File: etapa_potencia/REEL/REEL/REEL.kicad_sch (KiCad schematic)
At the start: 22 parts, among them SW1 SW_Push, SW2 SW_Reed, SW3 SW_Push, U2 ESP32-WROOM-32, U3 FT232

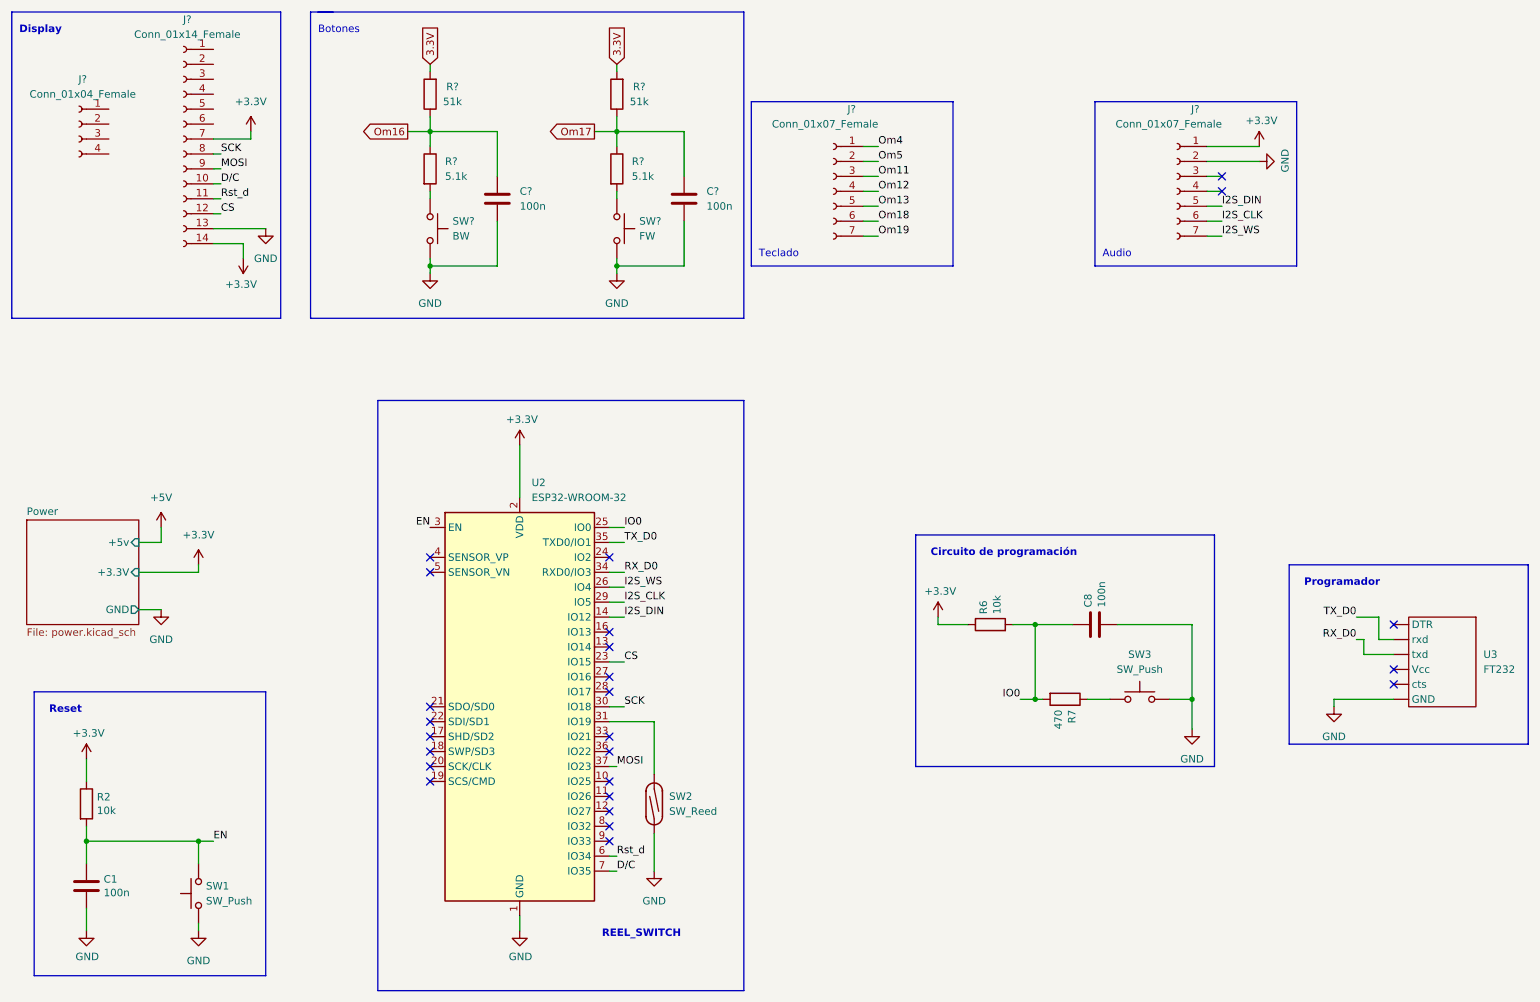
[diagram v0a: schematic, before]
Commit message: Edicion display y botones
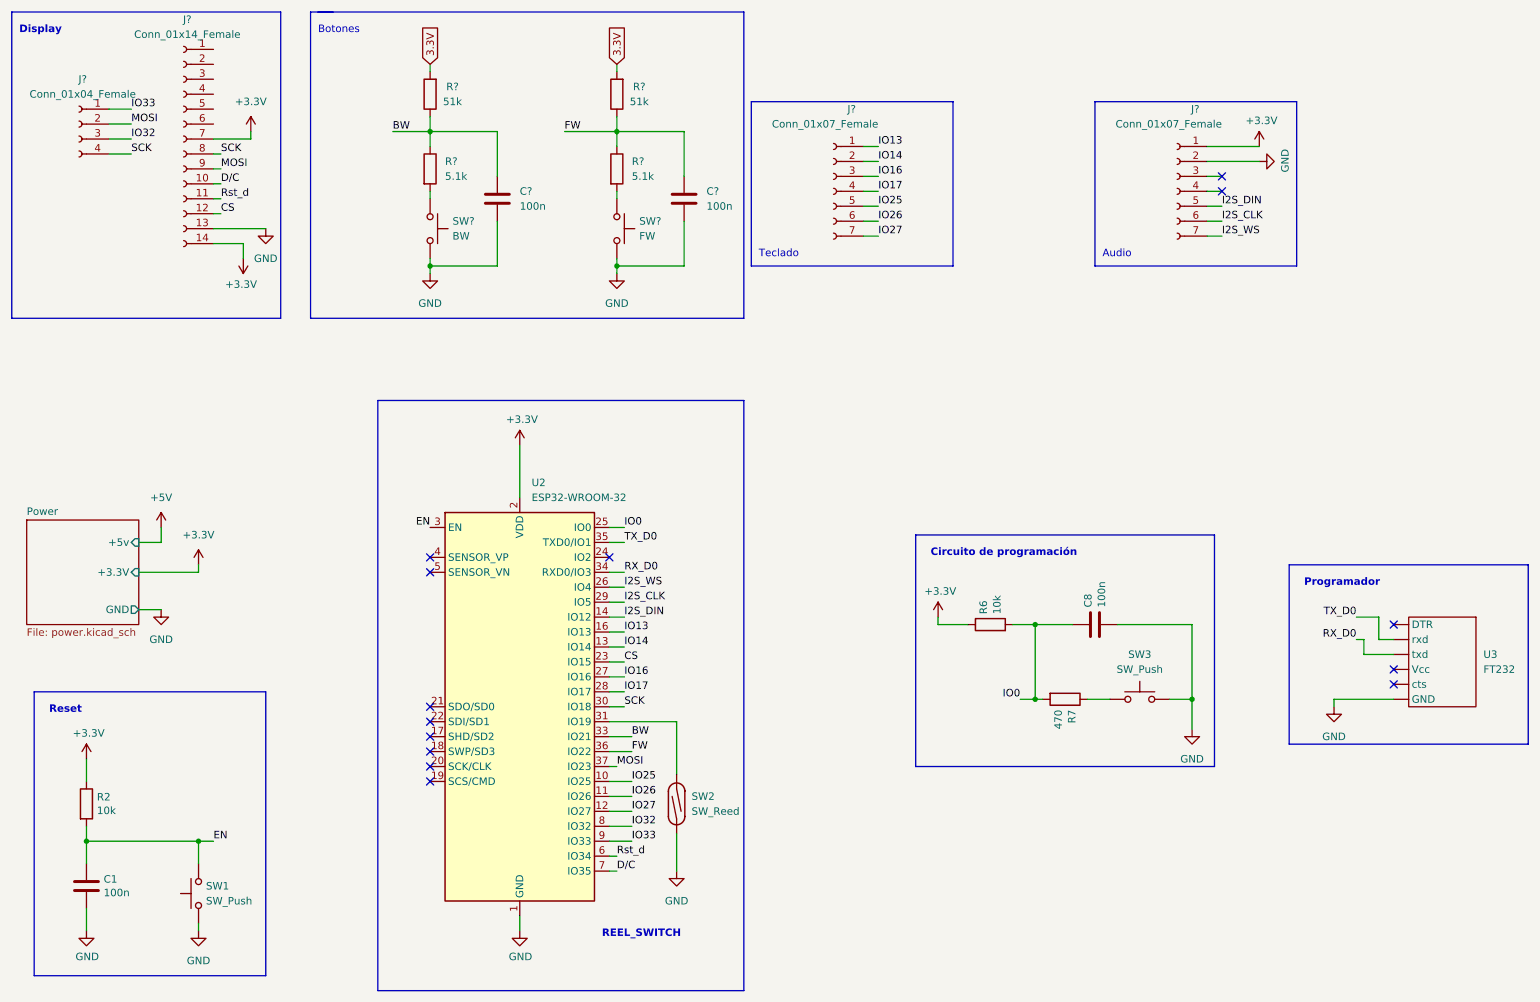
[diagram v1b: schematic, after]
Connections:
- net Om11 is gone; now on net IO16: J?.3 (Pin_3)
- net Om12 is gone; now on net IO17: J?.4 (Pin_4)
- net Om13 is gone; now on net IO25: J?.5 (Pin_5)
- net Om16 is gone; now on net BW: C?.2, R?.1, R?.1
- net Om17 is gone; now on net FW: C?.2, R?.1, R?.1
- net Om18 is gone; now on net IO26: J?.6 (Pin_6)
- net Om19 is gone; now on net IO27: J?.7 (Pin_7)
- net Om4 is gone; now on net IO13: J?.1 (Pin_1)
- net Om5 is gone; now on net IO14: J?.2 (Pin_2)
- net MOSI: now also J?.2 (Pin_2)
- net SCK: now also J?.4 (Pin_4)
- net IO25: now reaches U2.10 (IO25)
- net IO26: now reaches U2.11 (IO26)
- net IO27: now reaches U2.12 (IO27)
- net IO14: now reaches U2.13 (IO14)
- net IO13: now reaches U2.16 (IO13)
- net IO16: now reaches U2.27 (IO16)
- net IO17: now reaches U2.28 (IO17)
- net BW: now reaches U2.33 (IO21)
- net FW: now reaches U2.36 (IO22)
- net IO32: now reaches U2.8 (IO32)
- net IO32: now also J?.3 (Pin_3)
- net IO33: now reaches U2.9 (IO33)
- net IO33: now also J?.1 (Pin_1)
- no-connect marks 25 -> 14
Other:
- moved on the sheet: SW2

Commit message: Conexiones corregidas, PCB ordenada
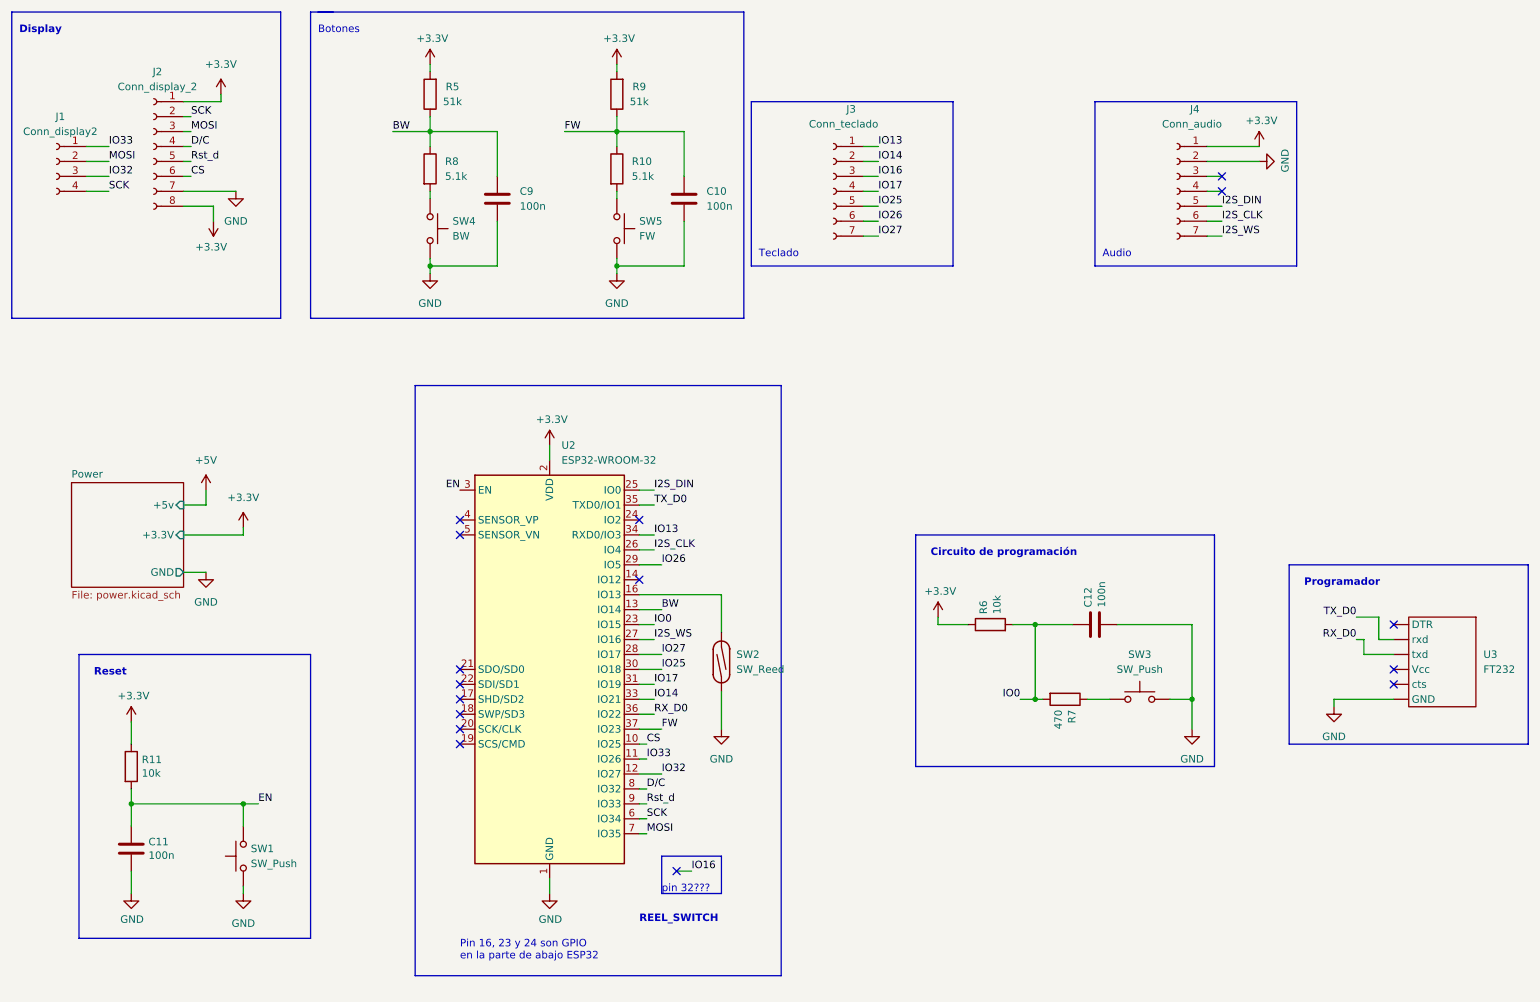
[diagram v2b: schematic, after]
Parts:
- removed J?: Conn_01x14_Female, Connector_PinSocket_2.54mm:PinSocket_1x14_P2.54mm_Vertical, symbol Connector:Conn_01x14_Female
- added J2: Conn_display_2, Connector_PinSocket_2.54mm:PinSocket_1x08_P2.54mm_Vertical, symbol Connector:Conn_01x08_Female
- J1: renamed from J?; value Conn_01x04_Female -> Conn_display2
- J3: renamed from J?; value Conn_01x07_Female -> Conn_teclado
- J4: renamed from J?; value Conn_01x07_Female -> Conn_audio
- gave numbers to parts that had none: 8
- renumbered C1 to C11, C8 to C12, R2 to R11
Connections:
- net 3.3V is gone; now on net +3V3: R5.2, R9.2
- net +3V3: now also J2.1 (Pin_1), J2.8 (Pin_8)
- net BW: now also U2.13 (IO14); no longer U2.33 (IO21)
- net CS: now also U2.10 (IO25), J2.6 (Pin_6); no longer U2.23 (IO15)
- net D/C: now also U2.8 (IO32), J2.4 (Pin_4); no longer U2.7 (IO35)
- net FW: now also U2.37 (IO23); no longer U2.36 (IO22)
- net GND: now also J2.7 (Pin_7)
- net I2S_CLK: now also U2.26 (IO4); no longer U2.29 (IO5)
- net I2S_DIN: now also U2.25 (IO0); no longer U2.14 (IO12)
- net I2S_WS: now also U2.27 (IO16); no longer U2.26 (IO4)
- net IO0: now also U2.23 (IO15); no longer U2.25 (IO0)
- net IO13: now also U2.34 (RXD0/IO3); no longer U2.16 (IO13)
- net IO14: now also U2.33 (IO21); no longer U2.13 (IO14)
- net IO16: no longer U2.27 (IO16)
- net IO17: now also U2.31 (IO19); no longer U2.28 (IO17)
- net IO25: now also U2.30 (IO18); no longer U2.10 (IO25)
- net IO26: now also U2.29 (IO5); no longer U2.11 (IO26)
- net IO27: now also U2.28 (IO17); no longer U2.12 (IO27)
- net IO32: now also U2.12 (IO27); no longer U2.8 (IO32)
- net IO33: now also U2.11 (IO26); no longer U2.9 (IO33)
- net MOSI: now also U2.7 (IO35), J2.3 (Pin_3); no longer U2.37 (IO23)
- net RX_D0: now also U2.36 (IO22); no longer U2.34 (RXD0/IO3)
- net Rst_d: now also U2.9 (IO33), J2.5 (Pin_5); no longer U2.6 (IO34)
- net SCK: now also U2.6 (IO34), J2.2 (Pin_2); no longer U2.30 (IO18)
- net at SW2.2: now also U2.16 (IO13); no longer U2.31 (IO19)
- no-connect marks 14 -> 16
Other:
- note added: "Pin 16, 23 y 24 son GPIO en la parte de abajo ESP32"
- note added: "pin 32???"
- moved on the sheet: C11, J1, R11, SW1, SW2, U2

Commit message: Primera organización huellas
Organización de huellas y conectores, falta parte de potencia
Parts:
- added C13: (no value), symbol Device:C
- C11, C12: footprint Capacitor_SMD:C_1210_3225Metric_Pad1.33x2.70mm_HandSolder -> Capacitor_SMD:C_0805_2012Metric_Pad1.18x1.45mm_HandSolder
- R11: footprint Resistor_SMD:R_1218_3246Metric_Pad1.22x4.75mm_HandSolder -> Resistor_SMD:R_0805_2012Metric_Pad1.20x1.40mm_HandSolder
- R6, R7: footprint Resistor_SMD:R_1218_3246Metric_Pad1.22x4.75mm_HandSolder -> (none)
- SW1: footprint Button_1825910-6:SW_1825910-6-4 -> TerminalBlock:TerminalBlock_Altech_AK300-2_P5.00mm
- SW3: footprint Button_1825910-6:SW_1825910-6-4 -> (none)
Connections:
- net +3V3: now also C13.2
- net GND: now also C13.1
- net I2S_DIN: now also U2.23 (IO15); no longer U2.25 (IO0)
- net IO16: no longer J3.3 (Pin_3)
- net RX_D0: now also U2.34 (RXD0/IO3); no longer U2.36 (IO22)
- net T3: now reaches U2.14 (IO12)
- net T3: now also J3.3 (Pin_3)
- net IO0 renamed Prom
- net Prom: now also U2.25 (IO0); no longer U2.23 (IO15)
- net IO13 renamed T1
- net T1: now also U2.36 (IO22); no longer U2.34 (RXD0/IO3)
- net IO14 renamed SDMISO
- net SDMISO: now also J1.3 (Pin_3); no longer J3.2 (Pin_2)
- net IO17 renamed T4
- net IO25 renamed T5
- net IO26 renamed T6
- net IO27 renamed T7
- net IO32 renamed T2
- net T2: now also J3.2 (Pin_2); no longer J1.3 (Pin_3)
- net IO33 renamed SDCS
- no-connect marks 16 -> 15
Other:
- sheet Power ports: added +5V; removed +5v
- note added: "Enable"
- note removed: "Reset"
- moved on the sheet: J3, J4

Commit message: Cambios en diagrama, separacion tierras, y capacitores
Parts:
- C13: value (none) -> 100n; footprint (none) -> Capacitor_SMD:C_0805_2012Metric_Pad1.18x1.45mm_HandSolder
- R6, R7: footprint (none) -> Resistor_SMD:R_0805_2012Metric_Pad1.20x1.40mm_HandSolder
- SW3: footprint (none) -> Button_Switch_SMD:SW_SPST_EVQQ2
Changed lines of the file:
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@@
       (effects (font (size 1.27 1.27)) (justify left))
     )
-    (property "Value" "" (id 1) (at 138.557 101.981 0)
-      (effects (font (size 1.27 1.27)) (justify left))
-    )
-    (property "Footprint" "" (id 2) (at 135.89 100.0252 0)
+    (property "Value" "100n" (id 1) (at 138.557 101.981 0)
+      (effects (font (size 1.27 1.27)) (justify left))
+    )
+    (property "Footprint" "Capacitor_SMD:C_0805_2012Metric_Pad1.18x1.45mm_HandSolder" (id 2) (at 135.89 100.0252 0)
       (effects (font (size 1.27 1.27)) hide)
     )
@@
       (effects (font (size 1.27 1.27)) (justify left))
     )
-    (property "Footprint" "" (id 2) (at 189.23 132.588 90)
+    (property "Footprint" "Resistor_SMD:R_0805_2012Metric_Pad1.20x1.40mm_HandSolder" (id 2) (at 189.23 132.588 90)
       (effects (font (size 1.27 1.27)) hide)
     )
@@
       (effects (font (size 1.27 1.27)) (justify left))
     )
-    (property "Footprint" "" (id 2) (at 201.93 141.732 90)
+    (property "Footprint" "Resistor_SMD:R_0805_2012Metric_Pad1.20x1.40mm_HandSolder" (id 2) (at 201.93 141.732 90)
       (effects (font (size 1.27 1.27)) hide)
     )
@@
     (property "Reference" "SW3" (id 0) (at 214.63 135.89 0))
     (property "Value" "SW_Push" (id 1) (at 214.63 138.43 0))
-    (property "Footprint" "" (id 2) (at 214.63 138.43 0)
+    (property "Footprint" "Button_Switch_SMD:SW_SPST_EVQQ2" (id 2) (at 214.63 138.43 0)
       (effects (font (size 1.27 1.27)) hide)
     )
@@
     )
     (path "/05689d2f-cd22-43d5-af77-23d23536e452/a15da288-795e-497a-8e6b-e8012bc97551"
-      (reference "BT1") (unit 1) (value "Battery_Cell") (footprint "Battery:BatteryHolder_Bulgin_BX0036_1xC")
+      (reference "BT1") (unit 1) (value "Battery_Cell") (footprint "Connector_JST:JST_PH_B2B-PH-K_1x02_P2.00mm_Vertical")
     )
     (path "/05689d2f-cd22-43d5-af77-23d23536e452/39e5100f-b93c-4f03-87cc-9280a7807294"
@@
     )
     (path "/05689d2f-cd22-43d5-af77-23d23536e452/3440893e-dd5e-44a2-9a99-1d8a5c359996"
-      (reference "C7") (unit 1) (value "10u") (footprint "Capacitor_SMD:C_1210_3225Metric_Pad1.33x2.70mm_HandSolder")
+      (reference "C7") (unit 1) (value "22u") (footprint "Capacitor_SMD:C_1210_3225Metric_Pad1.33x2.70mm_HandSolder")
     )
     (path "/05689d2f-cd22-43d5-af77-23d23536e452/9cc770d7-d3ea-4e39-94f0-5f75124434c2"
-      (reference "C8") (unit 1) (value "10u") (footprint "Capacitor_SMD:C_1210_3225Metric_Pad1.33x2.70mm_HandSolder")
+      (reference "C8") (unit 1) (value "22u") (footprint "Capacitor_SMD:C_1210_3225Metric_Pad1.33x2.70mm_HandSolder")
     )
     (path "/a575abf6-6e95-48c3-8e55-35929dca1647"
@@
       (reference "C13") (unit 1) (value "100n") (footprint "Capacitor_SMD:C_0805_2012Metric_Pad1.18x1.45mm_HandSolder")
     )
+    (path "/05689d2f-cd22-43d5-af77-23d23536e452/9c06488a-e7bc-409e-8b31-f9e814d13255"
+      (reference "C14") (unit 1) (value "10u") (footprint "Capacitor_SMD:C_1210_3225Metric_Pad1.33x2.70mm_HandSolder")
+    )
+    (path "/05689d2f-cd22-43d5-af77-23d23536e452/9c8dc7da-839b-4553-b608-bf9b4656fdb8"
+      (reference "C_k1") (unit 1) (value "10u") (footprint "Capacitor_SMD:C_1210_3225Metric_Pad1.33x2.70mm_HandSolder")
+    )
     (path "/05689d2f-cd22-43d5-af77-23d23536e452/35a78d65-1e29-46bd-8b55-7351f4af17d9"
       (reference "D1") (unit 1) (value "Green") (footprint "LED_SMD:LED_0805_2012Metric_Pad1.15x1.40mm_HandSolder")
@@
     )
     (path "/05689d2f-cd22-43d5-af77-23d23536e452/aab30d57-8d85-47c7-ae63-d2d45eadd0c3"
-      (reference "L1") (unit 1) (value "10u") (footprint "Inductor_SMD:L_0805_2012Metric_Pad1.05x1.20mm_HandSolder")
+      (reference "L1") (unit 1) (value "10u") (footprint "Inductor_SMD:L_6.3x6.3_H3")
+    )
+    (path "/05689d2f-cd22-43d5-af77-23d23536e452/77006be8-e871-4875-98bd-df9b9f9c71da"
+      (reference "L2") (unit 1) (value "33u") (footprint "Inductor_SMD:L_6.3x6.3_H3")
     )
     (path "/05689d2f-cd22-43d5-af77-23d23536e452/ef1a709c-9475-46da-a092-4fc32162d398"

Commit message: modificaciones por caras
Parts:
- removed SW2: SW_Reed, Resistor_THT:R_Axial_DIN0309_L9.0mm_D3.2mm_P25.40mm_Horizontal, symbol Switch:SW_Reed
- added J6: (no value), symbol Connector:Conn_01x02_Male
- U3: footprint Connector_PinHeader_2.54mm:PinHeader_1x06_P2.54mm_Vertical -> Connector_PinSocket_2.54mm:PinSocket_1x06_P2.54mm_Vertical
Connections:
- net GND: now also U3.6 (GND); no longer U3. (Vcc)
- net RX_D0: now also U3.3 (txd); no longer U3. (Vcc)
- net TX_D0: now also U3.2 (rxd); no longer U3. (Vcc)
- no-connect marks 15 -> 18

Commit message: etapa_audio
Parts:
- J6: value (none) -> Salida_audio; footprint (none) -> Connector_PinSocket_2.54mm:PinSocket_1x02_P2.54mm_Vertical
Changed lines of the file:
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@@
     (in_bom yes) (on_board yes) (fields_autoplaced)
     (property "Reference" "J6" (id 0) (at 194.945 36.83 0))
-    (property "Value" "" (id 1) (at 194.945 39.37 0))
-    (property "Footprint" "" (id 2) (at 194.31 41.91 0)
+    (property "Value" "Salida_audio" (id 1) (at 194.945 39.37 0))
+    (property "Footprint" "Connector_PinSocket_2.54mm:PinSocket_1x02_P2.54mm_Vertical" (id 2) (at 194.31 41.91 0)
       (effects (font (size 1.27 1.27)) hide)
     )
@@
     )
     (path "/bf82bd02-e1c6-44ee-9add-c1a616799e9b"
-      (reference "J6") (unit 1) (value "Conn_01x02_Male") (footprint "Connector_PinSocket_2.54mm:PinSocket_1x02_P2.54mm_Vertical")
+      (reference "J6") (unit 1) (value "Salida_audio") (footprint "Connector_PinSocket_2.54mm:PinSocket_1x02_P2.54mm_Vertical")
     )
     (path "/05689d2f-cd22-43d5-af77-23d23536e452/aab30d57-8d85-47c7-ae63-d2d45eadd0c3"

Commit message: Reorganización pcb
Después de primera revisión del profe Camargo
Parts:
- added J7: Entrada_buzzer, Connector_JST:JST_EH_B2B-EH-A_1x02_P2.50mm_Vertical, symbol Connector:Conn_01x02_Male
- J1: footprint Connector_PinSocket_2.54mm:PinSocket_1x04_P2.54mm_Vertical -> Connector_JST:JST_EH_B4B-EH-A_1x04_P2.50mm_Vertical
- J2: footprint Connector_PinSocket_2.54mm:PinSocket_1x08_P2.54mm_Vertical -> Connector_JST:JST_EH_B8B-EH-A_1x08_P2.50mm_Vertical
- J3: footprint Connector_PinSocket_2.54mm:PinSocket_1x07_P2.54mm_Vertical -> Connector_JST:JST_EH_B7B-EH-A_1x07_P2.50mm_Vertical
- J6: value Salida_audio -> Salida_amp
- R6: footprint Resistor_SMD:R_0805_2012Metric_Pad1.20x1.40mm_HandSolder -> (none)
- SW1: footprint TerminalBlock:TerminalBlock_Altech_AK300-2_P5.00mm -> (none)
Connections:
- net SD_MODE: now reaches U2.16 (IO13)
- net SD_MODE: now also J4.3 (Pin_3)
- net at J6.1 (Pin_1): now also J7.1 (Pin_1)
- net at J6.2 (Pin_2): now also J7.2 (Pin_2)
- no-connect marks 18 -> 14
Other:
- moved on the sheet: J4, J6
